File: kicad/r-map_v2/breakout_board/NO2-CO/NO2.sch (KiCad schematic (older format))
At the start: 29 parts, among them P1 CONN_01X05, P2 CONN_01X05, Q1 2N7002, Q2 2N7002, Q3 2N7002, Q4 2N7002, Q5 2N7002, Q6 2N7002, Q7 BC849, Q8 BC849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

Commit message: Schematic correction for DRC check
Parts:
- D1: Spice_Lib_File (none) -> LM4040_NA2P048_TRANS.lib; Spice_Model (none) -> LM4040; Spice_Netlist_Enabled (none) -> Y; Spice_Primitive (none) -> D
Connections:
- net labels added: HEATING
- net labels removed: N02
- wire segments 113 -> 100
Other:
- moved on the sheet: R1

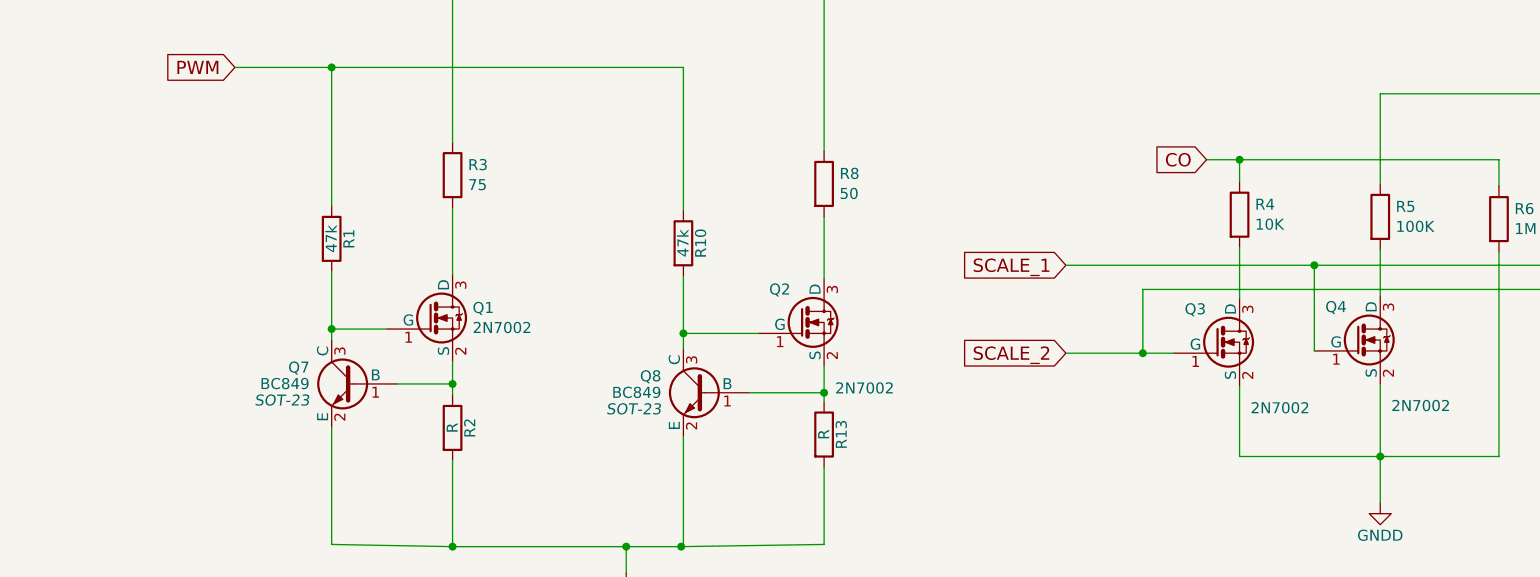
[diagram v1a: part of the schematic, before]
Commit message: New PCB board for NO2CO breakout
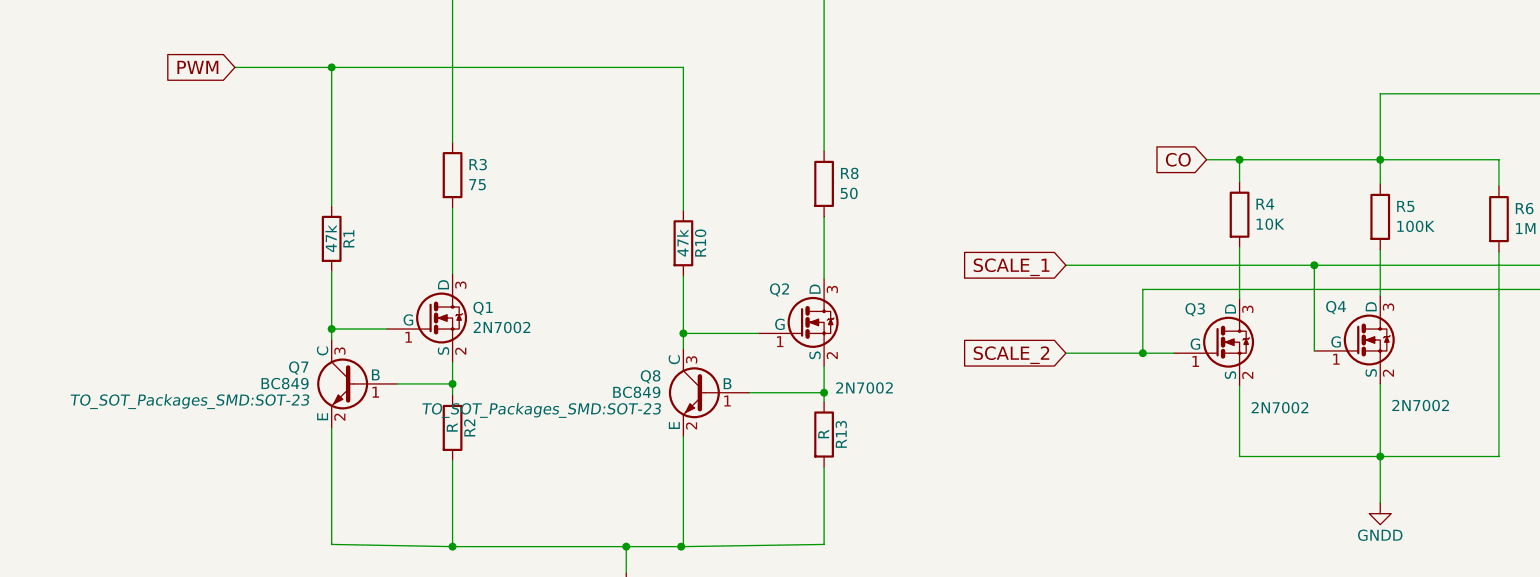
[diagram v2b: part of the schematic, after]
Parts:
- D1: footprint (none) -> TO_SOT_Packages_SMD:SOT-23
- Q7, Q8: footprint SOT-23 -> TO_SOT_Packages_SMD:SOT-23
- R1, R10, R13, R14, R15, R2, R7: footprint (none) -> Resistors_SMD:R_0805_HandSoldering
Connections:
- net CO: now also R5.1, U1.3 (B)
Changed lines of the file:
@@
 F 0 "R7" V 8380 1180 50  0000 C CNN
 F 1 "560" V 8300 1180 50  0000 C CNN
-F 2 "" V 8230 1180 50  0000 C CNN
+F 2 "Resistors_SMD:R_0805_HandSoldering" V 8230 1180 50  0001 C CNN
 F 3 "" H 8300 1180 50  0000 C CNN
 	1    8300 1180
@@
 F 0 "D1" H 8300 1980 50  0000 C CNN
 F 1 "ZENER" H 8300 1780 50  0000 C CNN
-F 2 "" H 8300 1880 50  0000 C CNN
+F 2 "TO_SOT_Packages_SMD:SOT-23" H 8300 1880 50  0001 C CNN
 F 3 "" H 8300 1880 50  0000 C CNN
 F 4 "D" H 8300 1880 60  0001 C CNN "Spice_Primitive"
@@
 F 0 "R14" V 5520 1630 50  0000 C CNN
 F 1 "100" V 5440 1630 50  0000 C CNN
-F 2 "" V 5370 1630 50  0000 C CNN
+F 2 "Resistors_SMD:R_0805_HandSoldering" V 5370 1630 50  0001 C CNN
 F 3 "" H 5440 1630 50  0000 C CNN
 	1    5440 1630
@@
 F 0 "R15" V 5530 2080 50  0000 C CNN
 F 1 "100" V 5450 2080 50  0000 C CNN
-F 2 "" V 5380 2080 50  0000 C CNN
+F 2 "Resistors_SMD:R_0805_HandSoldering" V 5380 2080 50  0001 C CNN
 F 3 "" H 5450 2080 50  0000 C CNN
 	1    5450 2080
@@
 F 0 "R13" V 3760 5890 50  0000 C CNN
 F 1 "R" V 3680 5890 50  0000 C CNN
-F 2 "" V 3610 5890 50  0000 C CNN
+F 2 "Resistors_SMD:R_0805_HandSoldering" V 3610 5890 50  0001 C CNN
 F 3 "" H 3680 5890 50  0000 C CNN
 	1    3680 5890
@@
 F 0 "R2" V 2070 5860 50  0000 C CNN
 F 1 "R" V 1990 5860 50  0000 C CNN
-F 2 "" V 1920 5860 50  0000 C CNN
+F 2 "Resistors_SMD:R_0805_HandSoldering" V 1920 5860 50  0001 C CNN
 F 3 "" H 1990 5860 50  0000 C CNN
 	1    1990 5860
@@
 F 0 "R10" V 3120 5020 50  0000 C CNN
 F 1 "47k" V 3040 5020 50  0000 C CNN
-F 2 "" V 2970 5020 50  0000 C CNN
+F 2 "Resistors_SMD:R_0805_HandSoldering" V 2970 5020 50  0001 C CNN
 F 3 "" H 3040 5020 50  0000 C CNN
 	1    3040 5020
@@
 F 0 "R1" V 1520 5000 50  0000 C CNN
 F 1 "47k" V 1440 5000 50  0000 C CNN
-F 2 "" V 1370 5000 50  0000 C CNN
+F 2 "Resistors_SMD:R_0805_HandSoldering" V 1370 5000 50  0001 C CNN
 F 3 "" H 1440 5000 50  0000 C CNN
 	1    1440 5000
@@
 F 0 "Q7" H 1740 5735 50  0000 L CNN
 F 1 "BC849" H 1740 5660 50  0000 L CNN
-F 2 "SOT-23" H 1740 5585 50  0000 L CIN
+F 2 "TO_SOT_Packages_SMD:SOT-23" H 1740 5585 50  0000 L CIN
 F 3 "" H 1540 5660 50  0000 L CNN
 	1    1540 5660
@@
 F 0 "Q8" H 3340 5775 50  0000 L CNN
 F 1 "BC849" H 3340 5700 50  0000 L CNN
-F 2 "SOT-23" H 3340 5625 50  0000 L CIN
+F 2 "TO_SOT_Packages_SMD:SOT-23" H 3340 5625 50  0000 L CIN
 F 3 "" H 3140 5700 50  0000 L CNN
 	1    3140 5700
@@
 Text Label 9350 1280 1    60   ~ 0
 HEATING
+Connection ~ 6210 4640
 $EndSCHEMATC

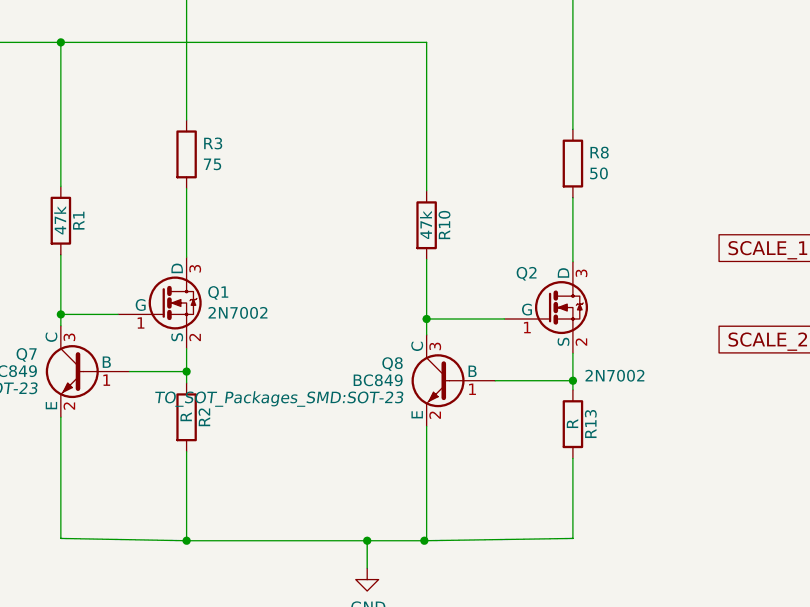
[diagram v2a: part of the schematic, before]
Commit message: complete the NO2-CO boards
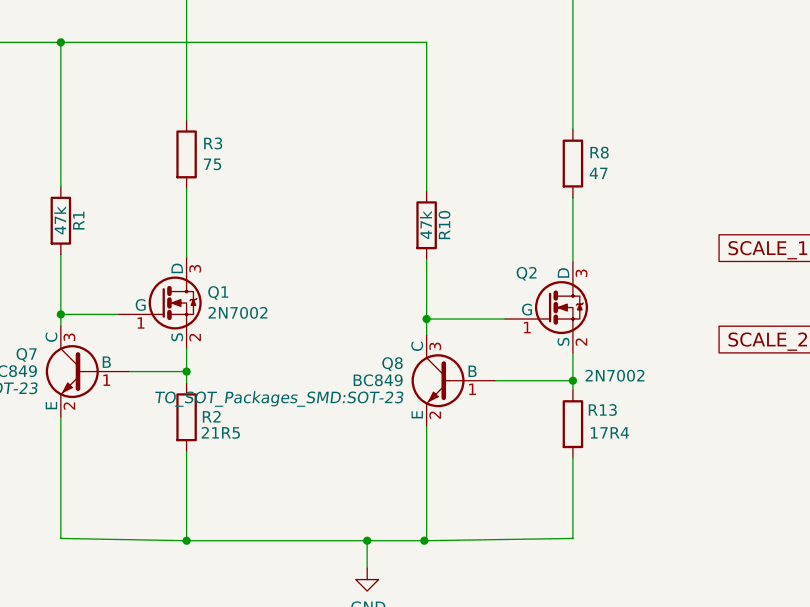
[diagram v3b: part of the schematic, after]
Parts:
- R13: value R -> 17R4
- R2: value R -> 21R5
- R8: value 50 -> 47
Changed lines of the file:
@@
 LIBS:mics-4514
 LIBS:NO2-cache
-EELAYER 26 0
+EELAYER 25 0
 EELAYER END
 $Descr A4 11693 8268
@@
 P 3680 4750
 F 0 "R8" H 3750 4796 50  0000 L CNN
-F 1 "50" H 3750 4705 50  0000 L CNN
+F 1 "47" H 3750 4705 50  0000 L CNN
 F 2 "Resistors_SMD:R_0805_HandSoldering" V -3990 550 50  0001 C CNN
 F 3 "" H -3920 550 50  0001 C CNN
@@
 U 1 1 589E9B0D
 P 3680 5890
-F 0 "R13" V 3760 5890 50  0000 C CNN
-F 1 "R" V 3680 5890 50  0000 C CNN
+F 0 "R13" H 3810 5950 50  0000 C CNN
+F 1 "17R4" H 3840 5850 50  0000 C CNN
 F 2 "Resistors_SMD:R_0805_HandSoldering" V 3610 5890 50  0001 C CNN
 F 3 "" H 3680 5890 50  0000 C CNN
@@
 U 1 1 589E9BBE
 P 1990 5860
-F 0 "R2" V 2070 5860 50  0000 C CNN
-F 1 "R" V 1990 5860 50  0000 C CNN
+F 0 "R2" H 2100 5860 50  0000 C CNN
+F 1 "21R5" H 2140 5790 50  0000 C CNN
 F 2 "Resistors_SMD:R_0805_HandSoldering" V 1920 5860 50  0001 C CNN
 F 3 "" H 1990 5860 50  0000 C CNN

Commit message: Board correction for MICS-4514 bad pinout. Correction for Stima_AirQuality_Connector connector pinout
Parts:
- Q1, Q2, Q3, Q4, Q5, Q6: symbol 2N7002 -> 2N7002-RESCUE-NO2
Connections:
- wire segments 100 -> 99
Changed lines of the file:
@@
 EESchema Schematic File Version 2
+LIBS:NO2-rescue
 LIBS:power
 LIBS:device
@@
 LIBS:mics-4514
 LIBS:NO2-cache
-EELAYER 25 0
+EELAYER 26 0
 EELAYER END
 $Descr A4 11693 8268
@@
 $EndComp
 $Comp
-L 2N7002 Q1
+L 2N7002-RESCUE-NO2 Q1
 U 1 1 5890F594
 P 1890 5360
@@
 NO2
 $Comp
-L 2N7002 Q2
+L 2N7002-RESCUE-NO2 Q2
 U 1 1 58976B71
 P 3580 5380
@@
 $EndComp
 $Comp
-L 2N7002 Q6
+L 2N7002-RESCUE-NO2 Q6
 U 1 1 589DDECE
 P 9450 5480
@@
 $EndComp
 $Comp
-L 2N7002 Q5
+L 2N7002-RESCUE-NO2 Q5
 U 1 1 589DE112
 P 8800 5490
@@
 $EndComp
 $Comp
-L 2N7002 Q4
+L 2N7002-RESCUE-NO2 Q4
 U 1 1 589DFBED
 P 6110 5460
@@
 $EndComp
 $Comp
-L 2N7002 Q3
+L 2N7002-RESCUE-NO2 Q3
 U 1 1 589DFBF3
 P 5470 5470
@@
 F 0 "Q7" H 1740 5735 50  0000 L CNN
 F 1 "BC849" H 1740 5660 50  0000 L CNN
-F 2 "TO_SOT_Packages_SMD:SOT-23" H 1740 5585 50  0000 L CIN
+F 2 "TO_SOT_Packages_SMD:SOT-23" H 1740 5585 50  0001 L CIN
 F 3 "" H 1540 5660 50  0000 L CNN
 	1    1540 5660
@@
 F 0 "Q8" H 3340 5775 50  0000 L CNN
 F 1 "BC849" H 3340 5700 50  0000 L CNN
-F 2 "TO_SOT_Packages_SMD:SOT-23" H 3340 5625 50  0000 L CIN
+F 2 "TO_SOT_Packages_SMD:SOT-23" H 3340 5625 50  0001 L CIN
 F 3 "" H 3140 5700 50  0000 L CNN
 	1    3140 5700
@@
 Wire Wire Line
 	6210 4340 6210 4750
-Wire Wire Line
-	9550 2640 9550 4770
-Wire Wire Line
-	9550 3110 9550 3110
 Wire Wire Line
 	4780 5120 9250 5120
@@
 HEATING
 Connection ~ 6210 4640
+Wire Wire Line
+	9550 2640 9550 4770
 $EndSCHEMATC

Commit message: Change for issues #227 and issue #229
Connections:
- wire segments 99 -> 98
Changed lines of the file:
@@
 L GND #PWR01
 U 1 1 5890F906
-P 2780 6520
-F 0 "#PWR01" H -2120 2120 50  0001 C CNN
-F 1 "GND" H 2785 6347 50  0000 C CNN
-F 2 "" H -2120 2370 50  0001 C CNN
-F 3 "" H -2120 2370 50  0001 C CNN
-	1    2780 6520
+P 6210 6200
+F 0 "#PWR01" H 1310 1800 50  0001 C CNN
+F 1 "GND" H 6215 6027 50  0000 C CNN
+F 2 "" H 1310 2050 50  0001 C CNN
+F 3 "" H 1310 2050 50  0001 C CNN
+	1    6210 6200
 	1    0    0    -1
 $EndComp
@@
 SCALE_2
 Text GLabel 1620 1500 1    60   Input ~ 0
-CO
+NO2
 $Comp
 L PWR_FLAG #FLG04
@@
 $EndComp
 Text GLabel 8750 4660 0    60   Input ~ 0
-NO2
+CO
 Text GLabel 1470 1500 1    60   Input ~ 0
-NO2
+CO
 $Comp
 L 2N7002-RESCUE-NO2 Q2
@@
 $EndComp
 Text GLabel 5420 4640 0    60   Input ~ 0
-CO
+NO2
 $Comp
 L R R6
@@
 $EndComp
 $Comp
-L GNDD #PWR013
-U 1 1 589E82C7
-P 9550 6190
-F 0 "#PWR013" H 9550 5940 50  0001 C CNN
-F 1 "GNDD" H 9550 6040 50  0000 C CNN
-F 2 "" H 9550 6190 50  0000 C CNN
-F 3 "" H 9550 6190 50  0000 C CNN
-	1    9550 6190
-	1    0    0    -1
-$EndComp
-$Comp
-L GNDD #PWR014
-U 1 1 589E8483
-P 6210 6200
-F 0 "#PWR014" H 6210 5950 50  0001 C CNN
-F 1 "GNDD" H 6210 6050 50  0000 C CNN
-F 2 "" H 6210 6200 50  0000 C CNN
-F 3 "" H 6210 6200 50  0000 C CNN
-	1    6210 6200
-	1    0    0    -1
-$EndComp
-$Comp
 L R R13
 U 1 1 589E9B0D
@@
 Connection ~ 3680 5700
 Wire Wire Line
-	1440 5860 1440 6390
-Wire Wire Line
-	1440 6390 1990 6400
-Wire Wire Line
-	1990 6400 3040 6400
-Wire Wire Line
-	3030 6400 3680 6390
+	1440 5860 1440 6400
+Wire Wire Line
+	1440 6400 3040 6400
+Wire Wire Line
+	3030 6400 3680 6400
 Wire Wire Line
 	2780 6400 2780 6520
@@
 Connection ~ 1990 6400
 Wire Wire Line
-	3680 6390 3680 6040
+	3680 6400 3680 6040
 Connection ~ 2780 6400
 Wire Wire Line
@@
 Wire Wire Line
 	3680 3390 3680 4600
-$Comp
-L GNDD #PWR015
-U 1 1 589E215C
-P 8300 2580
-F 0 "#PWR015" H 8300 2330 50  0001 C CNN
-F 1 "GNDD" H 8300 2430 50  0000 C CNN
-F 2 "" H 8300 2580 50  0000 C CNN
-F 3 "" H 8300 2580 50  0000 C CNN
-	1    8300 2580
-	1    0    0    -1
-$EndComp
 $Comp
 L +5V #PWR016
@@
 Wire Wire Line
 	9550 2640 9550 4770
+$Comp
+L GNDD #PWR04
+U 1 1 59A5F609
+P 2780 6520
+F 0 "#PWR04" H 2780 6270 50  0001 C CNN
+F 1 "GNDD" H 2780 6370 50  0000 C CNN
+F 2 "" H 2780 6520 50  0000 C CNN
+F 3 "" H 2780 6520 50  0000 C CNN
+	1    2780 6520
+	1    0    0    -1
+$EndComp
+$Comp
+L GND #PWR07
+U 1 1 59A5F969
+P 9550 6190
+F 0 "#PWR07" H 4650 1790 50  0001 C CNN
+F 1 "GND" H 9555 6017 50  0000 C CNN
+F 2 "" H 4650 2040 50  0001 C CNN
+F 3 "" H 4650 2040 50  0001 C CNN
+	1    9550 6190
+	1    0    0    -1
+$EndComp
+$Comp
+L GND #PWR013
+U 1 1 59A5FEF0
+P 8300 2580
+F 0 "#PWR013" H 8350 2630 50  0001 C CNN
+F 1 "GND" H 8305 2407 50  0000 C CNN
+F 2 "" H -1850 -2420 50  0001 C CNN
+F 3 "" H -1850 -2420 50  0001 C CNN
+	1    8300 2580
+	1    0    0    -1
+$EndComp
 $EndSCHEMATC
